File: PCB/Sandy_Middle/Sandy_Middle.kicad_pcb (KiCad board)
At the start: 2 copper layers, 285 x 75.2 mm, 71 parts, among them J1 Conn_02x02_Top_Bottom, J2 Conn_02x02_Top_Bottom, J3 Conn_02x02_Top_Bottom

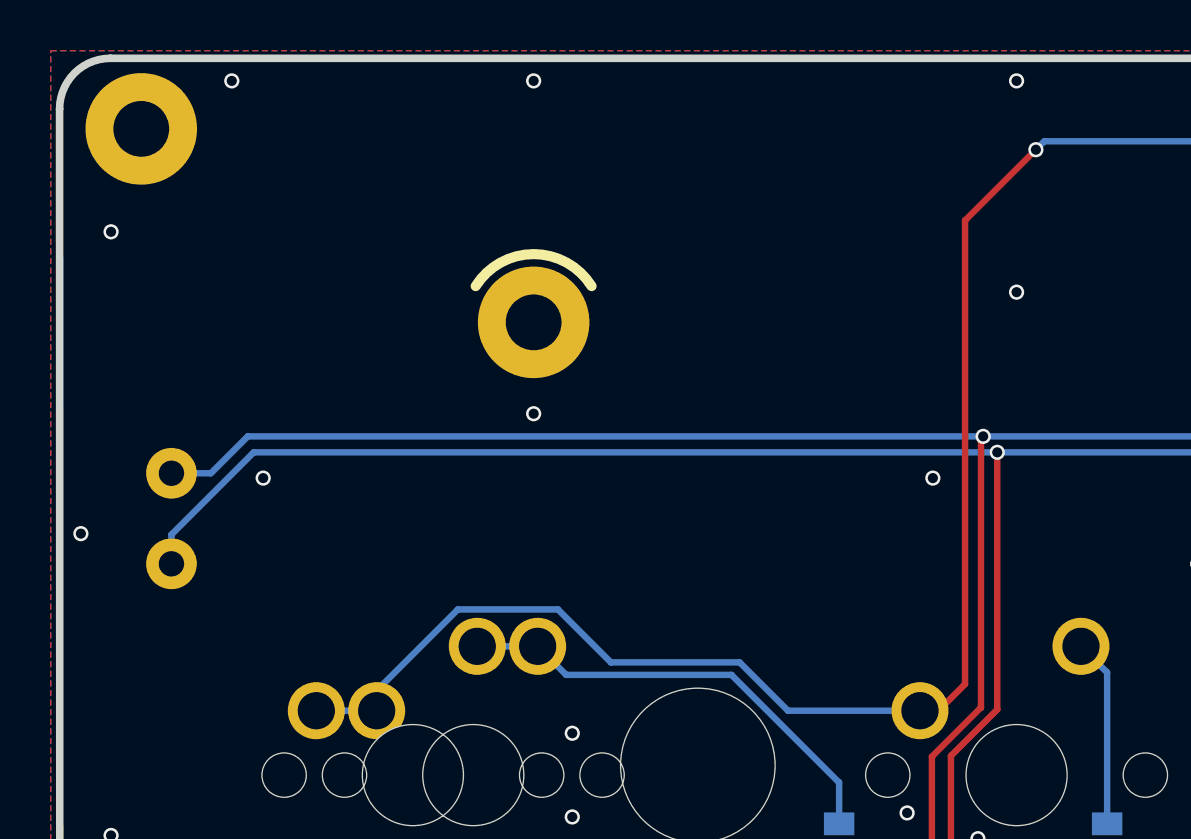
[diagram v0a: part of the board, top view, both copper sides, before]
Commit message: キーの間からEXT端子が見えないように移動した
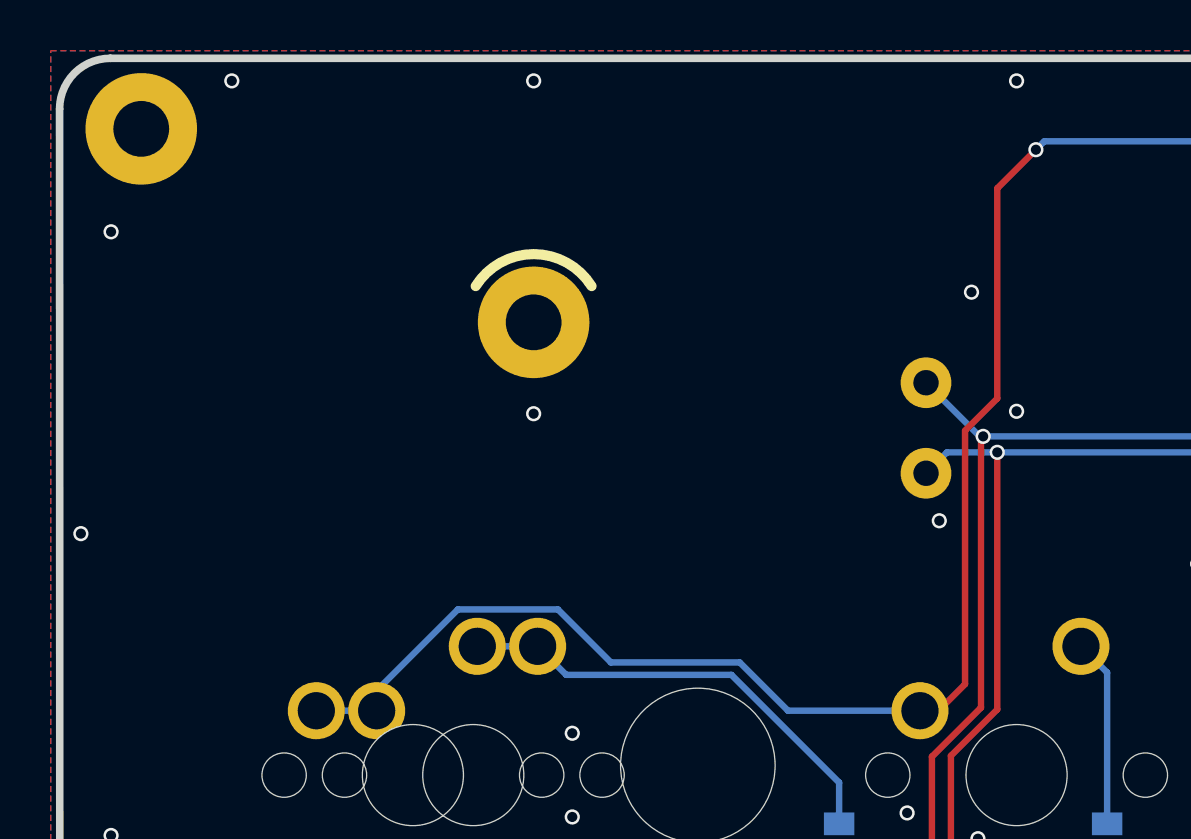
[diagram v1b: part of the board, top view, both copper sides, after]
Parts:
- moved EXT_MR1 30.0 mm to (55.6, 34.1)
- moved EXT_MR6 30.0 mm to (55.6, 37.7)
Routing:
- net Mid_row6: track 370.2 -> 338.3 mm
- net Mid_row1: track 352.7 -> 323.2 mm
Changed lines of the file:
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@@
   )
   (footprint "TestPoint:TestPoint_THTPad_D2.0mm_Drill1.0mm" (layer "B.Cu")
-    (at 25.820935 41.290905)
+    (at 55.58656 37.71903)
     (descr "THT pad as test Point, diameter 2.0mm, hole diameter 1.0mm")
     (tags "test point THT pad")
@@
   )
   (footprint "TestPoint:TestPoint_THTPad_D2.0mm_Drill1.0mm" (layer "B.Cu")
-    (at 25.820935 37.71903 180)
+    (at 55.58656 34.147155 180)
     (descr "THT pad as test Point, diameter 2.0mm, hole diameter 1.0mm")
     (tags "test point THT pad")
@@
   (segment (start 131.675435 60.42028) (end 132.310435 61.05528) (width 0.254) (layer "B.Cu") (net 8))
   (segment (start 52.158435 54.847155) (end 55.768207 54.847155) (width 0.254) (layer "B.Cu") (net 8))
+  (segment (start 57.703235 36.26383) (end 55.58656 34.147155) (width 0.254) (layer "B.Cu") (net 8))
   (segment (start 117.456735 36.26383) (end 57.84109 36.26383) (width 0.254) (layer "B.Cu") (net 8))
   (segment (start 55.768207 54.847155) (end 55.817231 54.798131) (width 0.254) (layer "B.Cu") (net 8))
@@
   (segment (start 263.51631 54.847155) (end 262.104435 53.43528) (width 0.254) (layer "B.Cu") (net 8))
   (segment (start 124.944435 46.560175) (end 124.944435 50.51428) (width 0.254) (layer "B.Cu") (net 8))
-  (segment (start 28.831885 36.26383) (end 27.376685 37.71903) (width 0.254) (layer "B.Cu") (net 8))
   (segment (start 148.947435 61.05528) (end 153.016735 65.12458) (width 0.254) (layer "B.Cu") (net 8))
+  (segment (start 57.84109 36.26383) (end 57.703235 36.26383) (width 0.254) (layer "B.Cu") (net 8))
   (segment (start 173.966435 64.10328) (end 174.913635 65.05048) (width 0.254) (layer "B.Cu") (net 8))
   (segment (start 272.28031 54.847155) (end 263.51631 54.847155) (width 0.254) (layer "B.Cu") (net 8))
@@
   (segment (start 187.079399 65.05048) (end 188.280597 63.849282) (width 0.254) (layer "B.Cu") (net 8))
   (segment (start 168.759435 64.10328) (end 173.966435 64.10328) (width 0.254) (layer "B.Cu") (net 8))
-  (segment (start 57.84109 36.26383) (end 28.831885 36.26383) (width 0.254) (layer "B.Cu") (net 8))
-  (segment (start 27.376685 37.71903) (end 25.820935 37.71903) (width 0.254) (layer "B.Cu") (net 8))
   (segment (start 132.310435 61.05528) (end 148.947435 61.05528) (width 0.254) (layer "B.Cu") (net 8))
   (segment (start 124.944435 50.51428) (end 120.61156 54.847155) (width 0.254) (layer "B.Cu") (net 8))
@@
   (via (at 203.430435 52.80028) (size 0.6) (drill 0.4) (layers "F.Cu" "B.Cu") (net 10))
   (segment (start 148.566435 61.56328) (end 152.757435 65.75428) (width 0.254) (layer "B.Cu") (net 10))
-  (segment (start 29.067372 36.89353) (end 25.820935 40.139967) (width 0.254) (layer "B.Cu") (net 10))
+  (segment (start 56.41206 36.89353) (end 55.58656 37.71903) (width 0.254) (layer "B.Cu") (net 10))
   (segment (start 129.414685 47.74403) (end 126.214685 47.74403) (width 0.254) (layer "B.Cu") (net 10))
   (segment (start 284.964435 42.48153) (end 288.012435 45.52953) (width 0.254) (layer "B.Cu") (net 10))
@@
   (segment (start 215.13031 54.847155) (end 214.27206 54.847155) (width 0.254) (layer "B.Cu") (net 10))
   (segment (start 215.114435 53.18128) (end 217.890436 50.405279) (width 0.254) (layer "B.Cu") (net 10))
-  (segment (start 25.820935 40.139967) (end 25.820935 41.290905) (width 0.254) (layer "B.Cu") (net 10))
   (segment (start 264.231685 36.98878) (end 269.724435 42.48153) (width 0.254) (layer "B.Cu") (net 10))
   (segment (start 217.890436 50.405279) (end 217.890436 38.594279) (width 0.254) (layer "B.Cu") (net 10))
@@
   (segment (start 168.948606 64.559981) (end 173.280136 64.559981) (width 0.254) (layer "B.Cu") (net 10))
   (segment (start 217.890436 38.594279) (end 219.495935 36.98878) (width 0.254) (layer "B.Cu") (net 10))
+  (segment (start 58.396435 36.89353) (end 56.41206 36.89353) (width 0.254) (layer "B.Cu") (net 10))
   (segment (start 296.09281 54.117905) (end 296.09281 54.847155) (width 0.254) (layer "B.Cu") (net 10))
   (segment (start 173.280136 64.559981) (end 174.474435 65.75428) (width 0.254) (layer "B.Cu") (net 10))
@@
   (segment (start 215.13031 54.847155) (end 215.114435 54.83128) (width 0.254) (layer "B.Cu") (net 10))
   (segment (start 269.724435 42.48153) (end 284.964435 42.48153) (width 0.254) (layer "B.Cu") (net 10))
-  (segment (start 58.396435 36.89353) (end 29.067372 36.89353) (width 0.254) (layer "B.Cu") (net 10))
   (segment (start 116.816435 36.89353) (end 58.396435 36.89353) (width 0.254) (layer "B.Cu") (net 10))
   (segment (start 288.012435 45.52953) (end 293.092435 45.52953) (width 0.254) (layer "B.Cu") (net 10))
@@
   (segment (start 148.45531 83.677155) (end 147.423435 82.64528) (width 0.254) (layer "B.Cu") (net 24))
   (segment (start 148.45531 89.647155) (end 148.45531 83.677155) (width 0.254) (layer "B.Cu") (net 24))
-  (segment (start 57.126435 27.74953) (end 59.920435 24.95553) (width 0.254) (layer "F.Cu") (net 25))
+  (segment (start 58.396435 26.47953) (end 59.920435 24.95553) (width 0.254) (layer "F.Cu") (net 25))
   (segment (start 55.348435 47.08528) (end 56.078685 47.08528) (width 0.254) (layer "F.Cu") (net 25))
+  (segment (start 57.126435 46.03753) (end 57.126435 36.03628) (width 0.254) (layer "F.Cu") (net 25))
+  (segment (start 58.396435 34.76628) (end 58.396435 26.47953) (width 0.254) (layer "F.Cu") (net 25))
   (segment (start 56.078685 47.08528) (end 57.126435 46.03753) (width 0.254) (layer "F.Cu") (net 25))
-  (segment (start 57.126435 46.03753) (end 57.126435 27.74953) (width 0.254) (layer "F.Cu") (net 25))
+  (segment (start 57.126435 36.03628) (end 58.396435 34.76628) (width 0.254) (layer "F.Cu") (net 25))
   (via (at 59.920435 24.95553) (size 0.6) (drill 0.4) (layers "F.Cu" "B.Cu") (net 25))
   (segment (start 201.652185 35.028405) (end 200.352185 35.028405) (width 0.254) (layer "B.Cu") (net 25))
@@
   (via (at 199.652185 75.81903) (size 0.6) (drill 0.4) (layers "F.Cu" "B.Cu") (free) (net 31))
   (via (at 78.208435 35.36953) (size 0.6) (drill 0.4) (layers "F.Cu" "B.Cu") (free) (net 31))
-  (via (at 55.856435 37.90953) (size 0.6) (drill 0.4) (layers "F.Cu" "B.Cu") (free) (net 31))
+  (via (at 59.158435 35.27428) (size 0.6) (drill 0.4) (layers "F.Cu" "B.Cu") (free) (net 31))
   (via (at 204.192435 50.60953) (size 0.6) (drill 0.4) (layers "F.Cu" "B.Cu") (free) (net 31))
   (via (at 159.996435 75.91428) (size 0.6) (drill 0.4) (layers "F.Cu" "B.Cu") (free) (net 31))
@@
   (via (at 257.532435 34.44878) (size 0.6) (drill 0.4) (layers "F.Cu" "B.Cu") (free) (net 31))
   (via (at 183.999435 71.59628) (size 0.6) (drill 0.4) (layers "F.Cu" "B.Cu") (free) (net 31))
-  (via (at 59.158435 30.57528) (size 0.6) (drill 0.4) (layers "F.Cu" "B.Cu") (free) (net 31))
+  (via (at 57.380435 30.57528) (size 0.6) (drill 0.4) (layers "F.Cu" "B.Cu") (free) (net 31))
   (via (at 119.864435 53.14953) (size 0.6) (drill 0.4) (layers "F.Cu" "B.Cu") (free) (net 31))
   (via (at 256.802185 38.06828) (size 0.6) (drill 0.4) (layers "F.Cu" "B.Cu") (free) (net 31))
@@
   (via (at 299.664685 56.76903) (size 0.6) (drill 0.4) (layers "F.Cu" "B.Cu") (free) (net 31))
   (via (at 204.954435 53.91153) (size 0.6) (drill 0.4) (layers "F.Cu" "B.Cu") (free) (net 31))
-  (via (at 29.440435 37.90953) (size 0.6) (drill 0.4) (layers "F.Cu" "B.Cu") (free) (net 31))
+  (via (at 56.110435 39.59228) (size 0.6) (drill 0.4) (layers "F.Cu" "B.Cu") (free) (net 31))
   (via (at 151.233435 76.42228) (size 0.6) (drill 0.4) (layers "F.Cu" "B.Cu") (free) (net 31))
   (via (at 268.200435 42.73553) (size 0.6) (drill 0.4) (layers "F.Cu" "B.Cu") (free) (net 31))
@@
     (polygon
       (pts
+        (xy 55.094435 37.71268)
+        (xy 54.230835 37.71268)
+        (xy 54.230835 34.10588)
+        (xy 55.094435 34.10588)
+      )
+    )
+  )
+  (zone (net 0) (net_name "") (layer "B.Cu") (hatch edge 0.508)
+    (connect_pads (clearance 0))
+    (min_thickness 0.254)
+    (keepout (tracks allowed) (vias allowed) (pads allowed) (copperpour not_allowed) (footprints allowed))
+    (fill (thermal_gap 0.508) (thermal_bridge_width 0.508))
+    (polygon
+      (pts
         (xy 176.506435 91.40828)
         (xy 173.458435 91.40828)
@@
       )
     )
-  )
-  (zone (net 0) (net_name "") (layer "B.Cu") (hatch edge 0.508)
-    (connect_pads (clearance 0))
-    (min_thickness 0.254)
-    (keepout (tracks allowed) (vias allowed) (pads allowed) (copperpour not_allowed) (footprints allowed))
-    (fill (thermal_gap 0.508) (thermal_bridge_width 0.508))
-    (polygon
-      (pts
-        (xy 15.89906 52.76853)
-        (xy 10.81906 52.76853)
-        (xy 8.78706 54.80053)
-        (xy 3.19906 49.62528)
-        (xy 15.89906 50.99053)
-      )
-    )

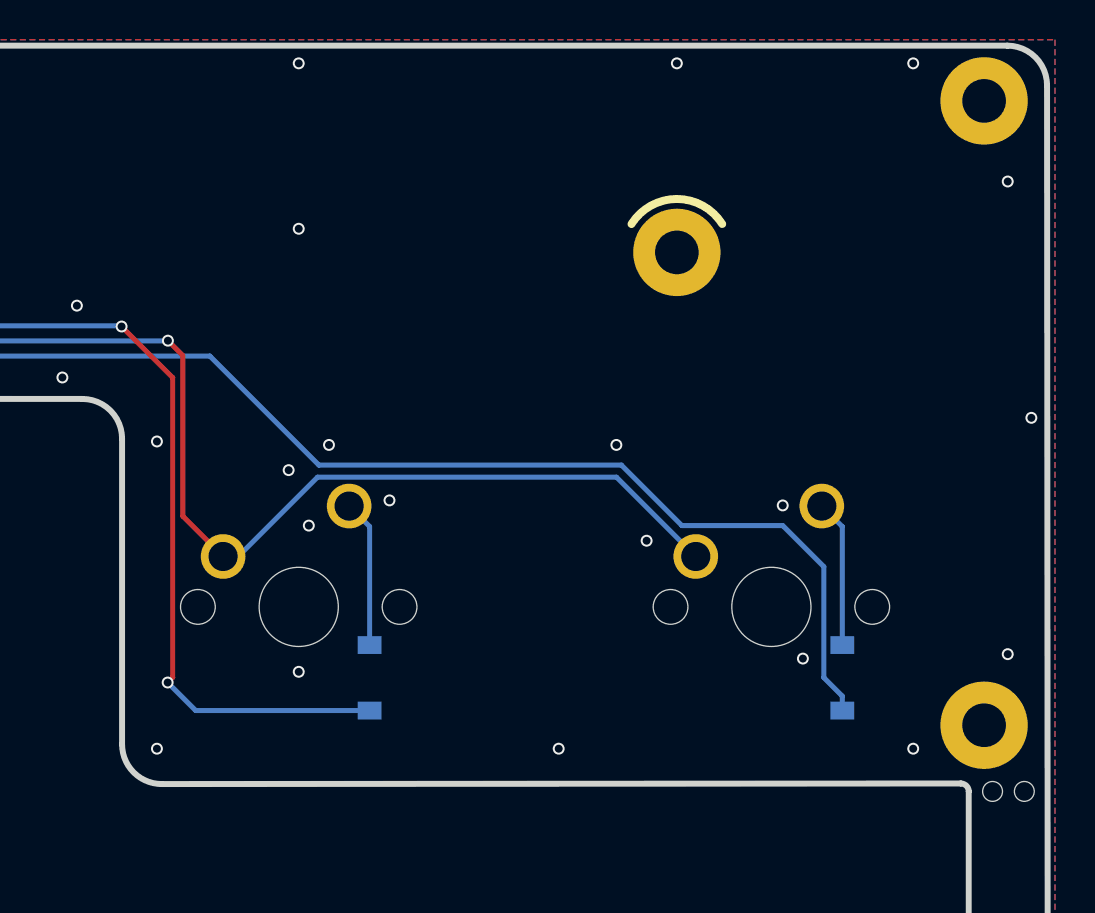
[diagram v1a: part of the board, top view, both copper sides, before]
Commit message: コネクタの接続先がわかるシルクを追加
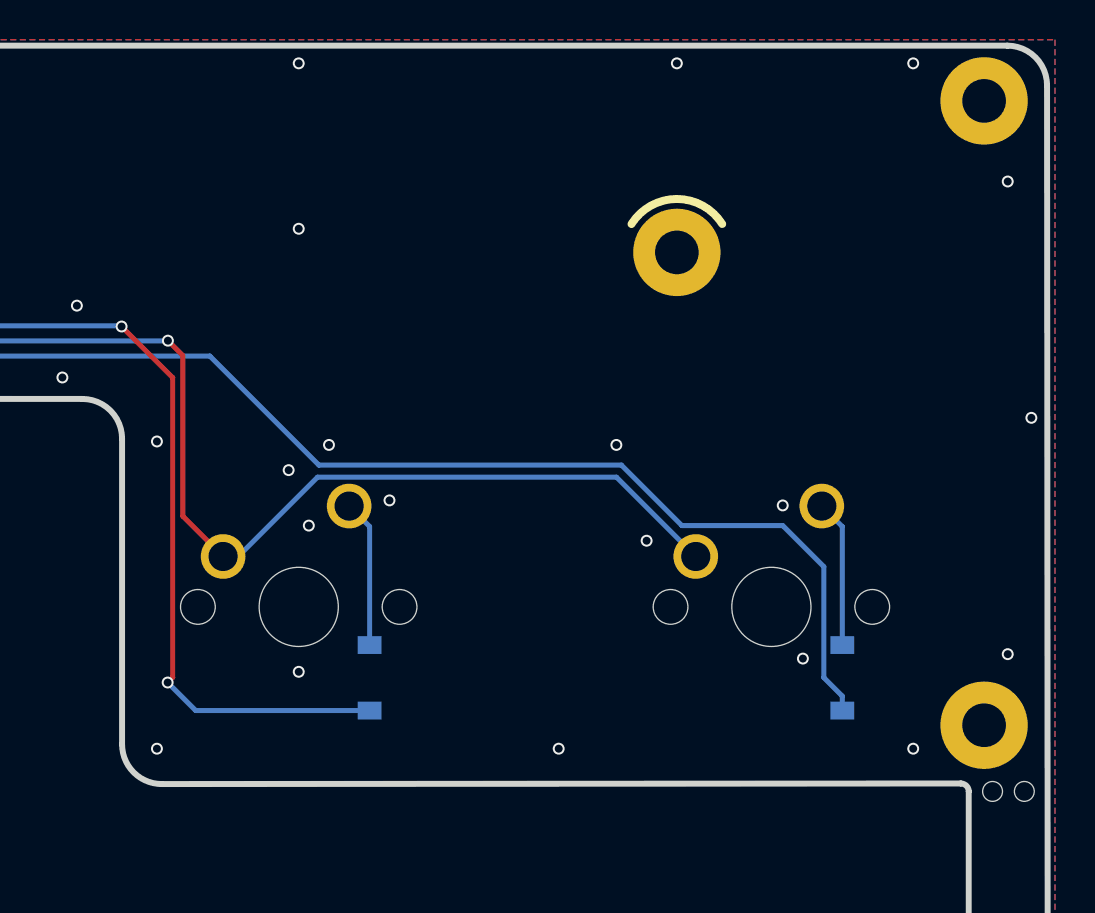
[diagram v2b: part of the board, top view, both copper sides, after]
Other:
- board text added: "Mid 1"
- board text added: "Mid 2"
- board text added: "Mid 3"

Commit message: "Back Side"シルク位置調整
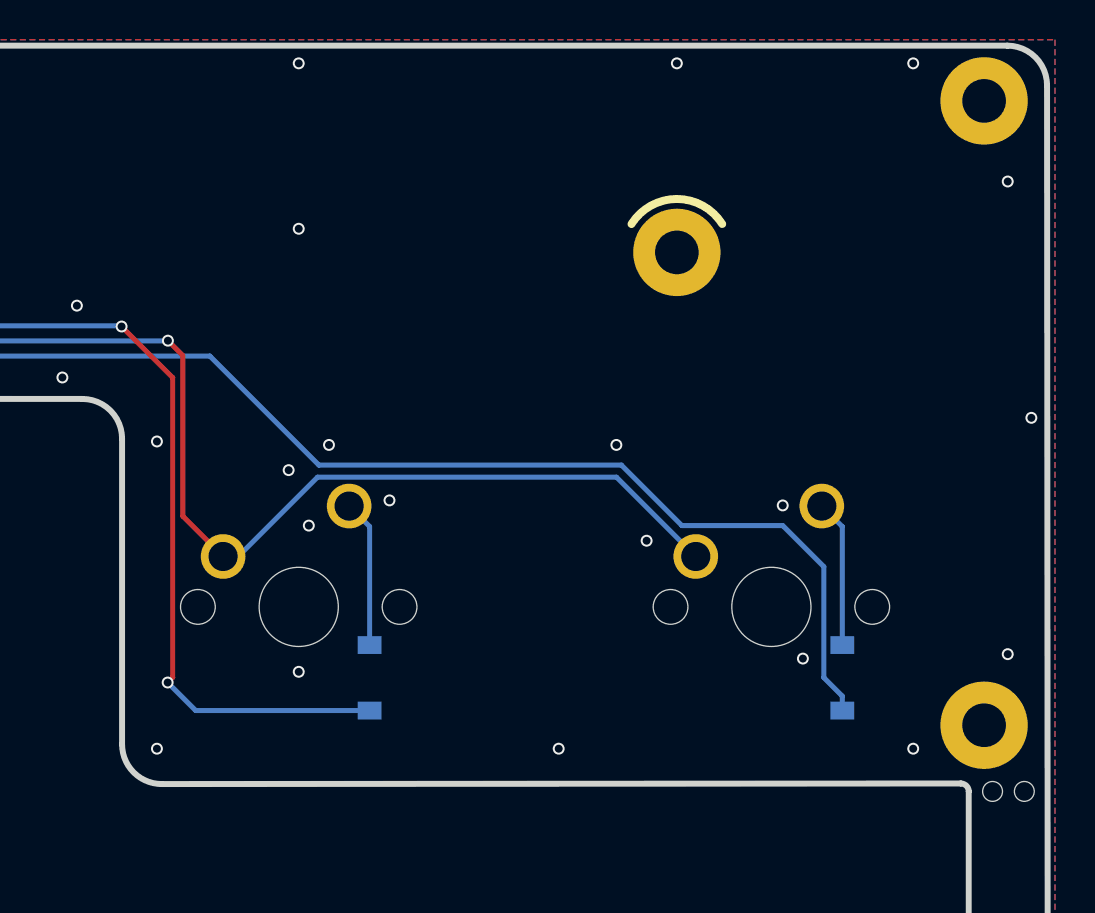
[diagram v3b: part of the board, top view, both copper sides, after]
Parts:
- removed G***: LOGO, Jones.local:Sandy_logo_w20

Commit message: コネクタの番号と、パーツの番号を合わせる
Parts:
- renumbered J2 to J1, J3 to J2, J1 to J3
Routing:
- net Mid_GND: vias 140 -> 139
